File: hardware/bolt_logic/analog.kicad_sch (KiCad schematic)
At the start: 40 parts, among them U10 LM2901, U11 74HCT4052, U7 MCP6292, U8 MCP6292, U9 LM2901

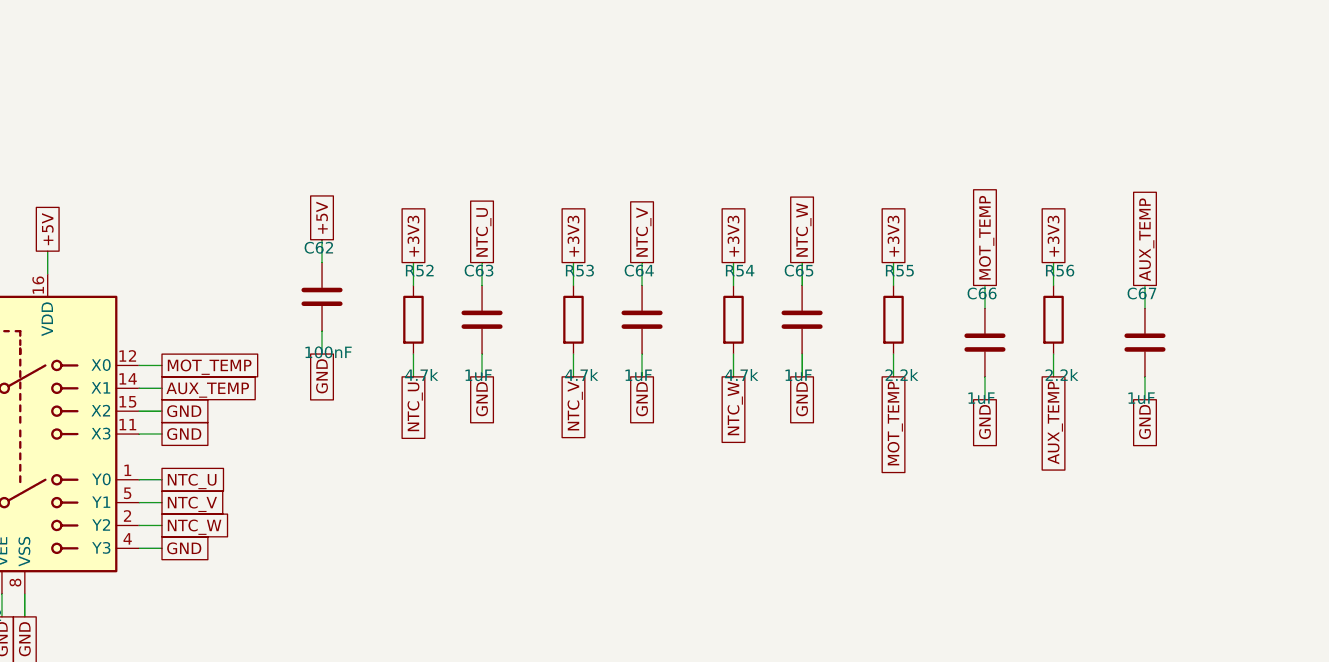
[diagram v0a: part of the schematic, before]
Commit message: Remove the aux header (J3) and V6 leftovers: only CN1, CN2 and programming
Owner: the only connections on the board are CN1, CN2 and what is needed
to program it (J1 SWD, J4 ESP32).

- Removed J3 and what only served it: aux 12 V / 5 V outputs (F3, F4),
  aux temperature pull-up and filter (R56, C67; mux 1Y1 grounded), the
  emergency-stop / motor-protection header resistors and caps (R110,
  R112, C105, C106; the 10k pull-ups stay, so the firmware reads OK).
- CN1 G1/G2 (HVIL) only went to J3: now reserved positions.
- PC11 (VTG_OUT) and PC5 (SPEED_OUT, never connected) now NC.
- Re-placed and re-routed: 241 parts, DRC 0 violations, 0 unconnected.
- Docs: 03 (pin map, 4.10, 4.12, 4.13, CN1 table), 04, 05 updated;
  SWD header described as the 5-pin part it is.

Co-Authored-By: Claude Opus 5.5 <noreply@anthropic.com>
Claude-Session: https://claude.ai/code/session_01KW1M8KfVLc83FDDiK2YEWM
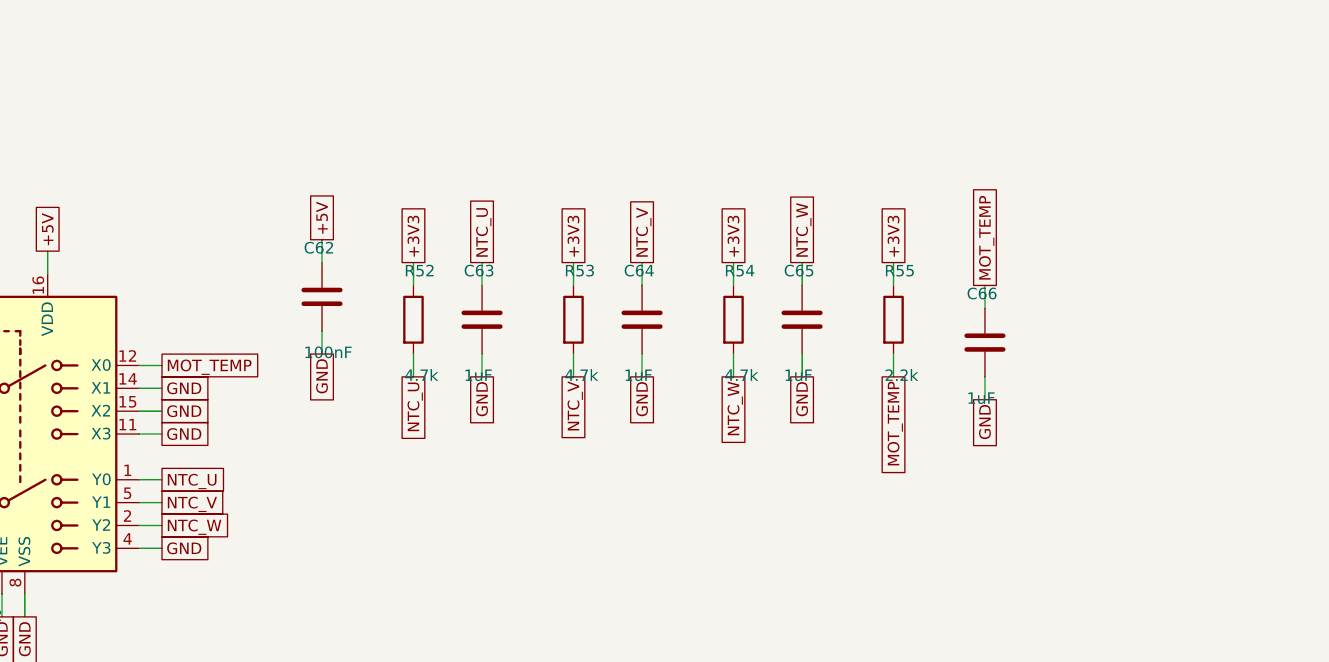
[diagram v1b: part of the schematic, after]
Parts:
- removed C67: 1uF, Capacitor_SMD:C_0805_2012Metric, symbol Device:C
- removed R56: 2.2k, Resistor_SMD:R_0805_2012Metric, symbol Device:R
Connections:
- net AUX_TEMP is gone; now on net GND: U11.14 (X1)
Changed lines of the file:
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@@
       (type default))
 )
-  (global_label "AUX_TEMP"
+  (global_label "GND"
     (shape passive)
     (at 63.5 139.7 0)
@@
     (property "Intersheetrefs" "${INTERSHEET_REFS}"
       (at 154.94 140.97 0)
-      (effects
-        (font (size 1.27 1.27)) hide)))
-  (wire
-    (pts
-      (xy 162.56 128.27)
-      (xy 162.56 125.73))
-    (stroke
-      (width 0)
-      (type default))
-)
-  (global_label "+3V3"
-    (shape passive)
-    (at 162.56 125.73 90)
-    (fields_autoplaced)
-    (effects
-      (font (size 1.27 1.27))
-      (justify left))
-    (property "Intersheetrefs" "${INTERSHEET_REFS}"
-      (at 162.56 125.73 0)
-      (effects
-        (font (size 1.27 1.27)) hide)))
-  (wire
-    (pts
-      (xy 162.56 135.89)
-      (xy 162.56 138.43))
-    (stroke
-      (width 0)
-      (type default))
-)
-  (global_label "AUX_TEMP"
-    (shape passive)
-    (at 162.56 138.43 270)
-    (fields_autoplaced)
-    (effects
-      (font (size 1.27 1.27))
-      (justify right))
-    (property "Intersheetrefs" "${INTERSHEET_REFS}"
-      (at 162.56 138.43 0)
-      (effects
-        (font (size 1.27 1.27)) hide)))
-  (wire
-    (pts
-      (xy 172.72 130.81)
-      (xy 172.72 128.27))
-    (stroke
-      (width 0)
-      (type default))
-)
-  (global_label "AUX_TEMP"
-    (shape passive)
-    (at 172.72 128.27 90)
-    (fields_autoplaced)
-    (effects
-      (font (size 1.27 1.27))
-      (justify left))
-    (property "Intersheetrefs" "${INTERSHEET_REFS}"
-      (at 172.72 128.27 0)
-      (effects
-        (font (size 1.27 1.27)) hide)))
-  (wire
-    (pts
-      (xy 172.72 138.43)
-      (xy 172.72 140.97))
-    (stroke
-      (width 0)
-      (type default))
-)
-  (global_label "GND"
-    (shape passive)
-    (at 172.72 140.97 270)
-    (fields_autoplaced)
-    (effects
-      (font (size 1.27 1.27))
-      (justify right))
-    (property "Intersheetrefs" "${INTERSHEET_REFS}"
-      (at 172.72 140.97 0)
       (effects
         (font (size 1.27 1.27)) hide)))
@@
   (path "/091edd89-91d5-54b9-892a-aa28117da9e5/f0d79f54-d87e-51e5-b897-d0534300d643"
     (reference "C66")
-    (unit 1)))))
-  (symbol
-    (lib_id "Device:R")
-    (at 162.56 132.08 0)
-    (unit 1)
-    (in_bom yes)
-    (on_board yes)
-    (dnp no)
-    (property "Reference" "R56"
-      (at 161.544 126.67 0)
-      (effects
-        (font (size 1.27 1.27))
-        (justify left)))
-    (property "Value" "2.2k"
-      (at 161.544 138.29 0)
-      (effects
-        (font (size 1.27 1.27))
-        (justify left)))
-    (property "Footprint" "Resistor_SMD:R_0805_2012Metric"
-      (at 162.56 132.08 0)
-      (effects
-        (font (size 1.27 1.27)) hide))
-    (property "Datasheet" "~"
-      (at 162.56 132.08 0)
-      (effects
-        (font (size 1.27 1.27)) hide))
-    (pin "1"
-)
-    (pin "2"
-)
-    (instances (project "bolt_logic"
-  (path "/091edd89-91d5-54b9-892a-aa28117da9e5/f0d79f54-d87e-51e5-b897-d0534300d643"
-    (reference "R56")
-    (unit 1)))))
-  (symbol
-    (lib_id "Device:C")
-    (at 172.72 134.62 0)
-    (unit 1)
-    (in_bom yes)
-    (on_board yes)
-    (dnp no)
-    (property "Reference" "C67"
-      (at 170.688 129.21 0)
-      (effects
-        (font (size 1.27 1.27))
-        (justify left)))
-    (property "Value" "1uF"
-      (at 170.688 140.83 0)
-      (effects
-        (font (size 1.27 1.27))
-        (justify left)))
-    (property "Footprint" "Capacitor_SMD:C_0805_2012Metric"
-      (at 172.72 134.62 0)
-      (effects
-        (font (size 1.27 1.27)) hide))
-    (property "Datasheet" "~"
-      (at 172.72 134.62 0)
-      (effects
-        (font (size 1.27 1.27)) hide))
-    (pin "1"
-)
-    (pin "2"
-)
-    (instances (project "bolt_logic"
-  (path "/091edd89-91d5-54b9-892a-aa28117da9e5/f0d79f54-d87e-51e5-b897-d0534300d643"
-    (reference "C67")
     (unit 1))))))
